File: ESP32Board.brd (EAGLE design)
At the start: 46 x 58 mm, 20 parts, among them J1 MICRO_USB_B_HIROSE_ZX62-B-5PA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, U2 CH340K

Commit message: Fix connection
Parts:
- removed J1: MICRO_USB_B_HIROSE_ZX62-B-5PA(11), connector:USB_MICRO_B-HIROSE-ZX62-B-5PA(11)
- added J2: MICRO_USB_B_HIROSE_ZX62-B-5PA(11)MODEL, connector:GHI-CONNECTORS_10118192-0001LF(MICRO-USB-B-AMPHENOL-FCI)
- R4: value 2k -> 470
- R5: value 2k -> 1k
- renumbered GLED to LED, RLED to POWER
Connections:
- net GND: now also J2.CGND1, J2.CGND2, J2.CGND3, J2.CGND4, J2.CGND5, J2.CGND6, J2.GND; no longer J1.5
- net UD+: now also J2.D+; no longer J1.3
- net UD-: now also J2.D-; no longer J1.2
- net USB5V: now also J2.VBUS; no longer J1.1
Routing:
- net IO33: track 54.4 -> 32.7 mm
- net IO26: track 46.8 -> 66.1 mm
- net GND: track 135.5 -> 149.5 mm, vias 23 -> 24
- net IO25: track 43.2 -> 37.8 mm
- net VCC: track 51.5 -> 56.5 mm
- net IO5: track 35.3 -> 30.5 mm
- net IO18: track 35.9 -> 33.4 mm
- net IO19: track 32.4 -> 31.2 mm
- net IO21: track 29.0 -> 28.5 mm
- net UD-: track 46.3 -> 46.8 mm

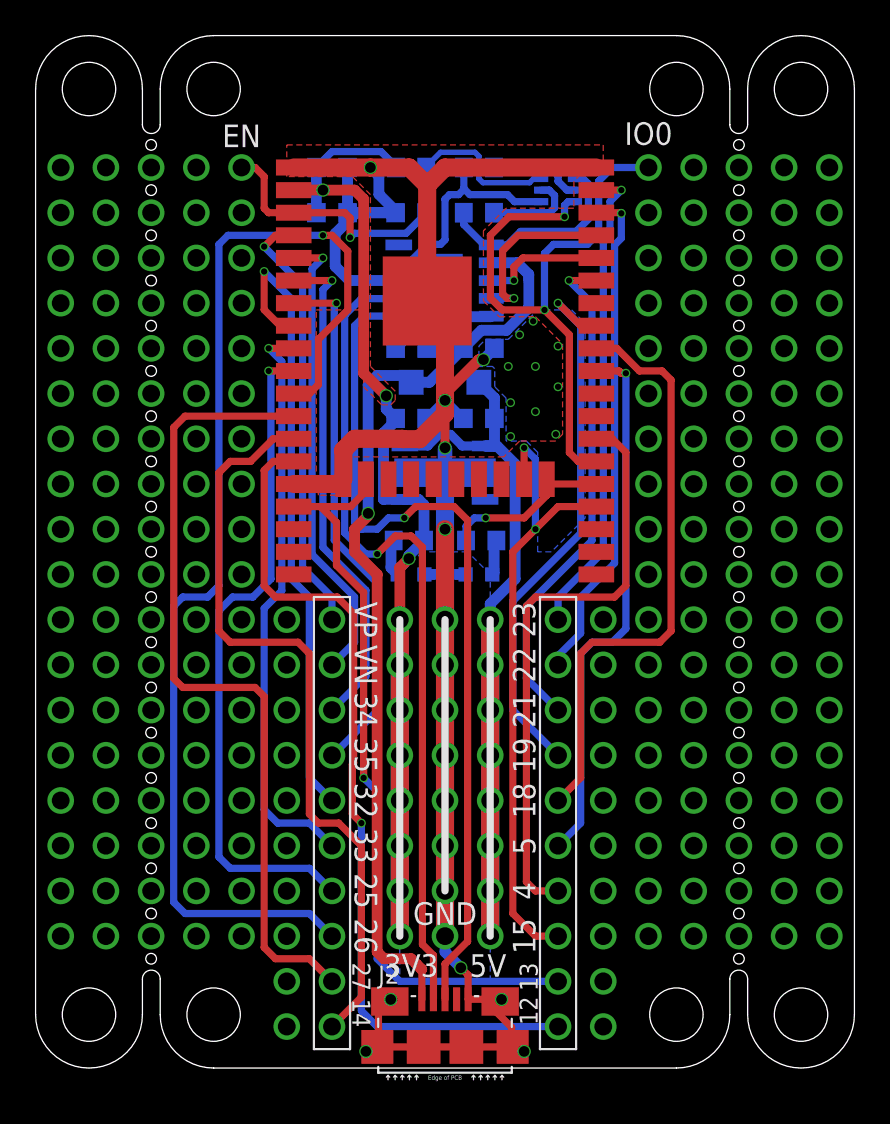
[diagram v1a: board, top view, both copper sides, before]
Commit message: Add reset switch
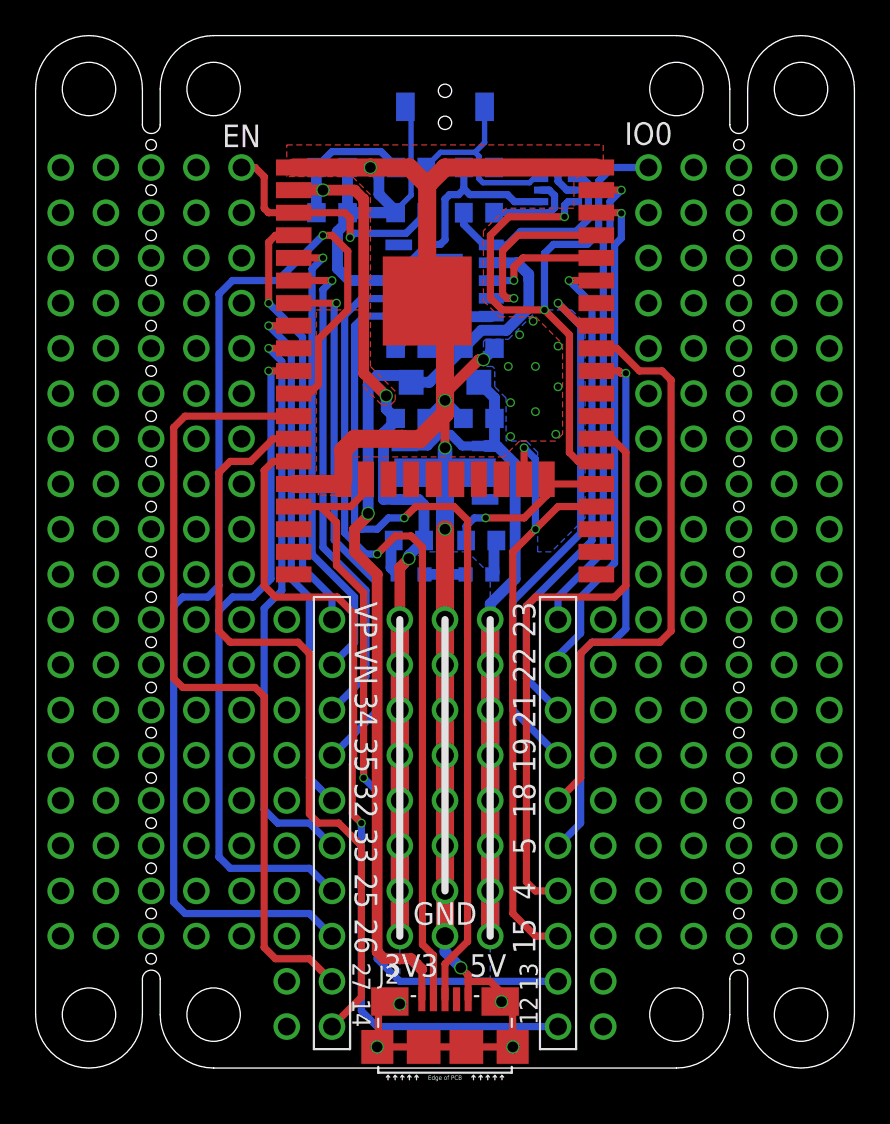
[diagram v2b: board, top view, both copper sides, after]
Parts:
- added U$2: TVAF06-A020B-R, switches:TVAF06-A020B-R
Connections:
- net EN: now also U$2.P$1
- net GND: now also U$2.P$2
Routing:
- net GND: track 149.5 -> 157.1 mm, vias 24 -> 28
- net IO32: track 35.5 -> 29.5 mm
- net EN: track 25.2 -> 28.0 mm
- net IO26: track 66.1 -> 64.5 mm
